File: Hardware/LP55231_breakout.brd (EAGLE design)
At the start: 22.9 x 30.5 mm, 29 parts, among them J1 To micro, J2 USER LED, J3 USER LED, J4 USER LED, U1 LP55231WQFN

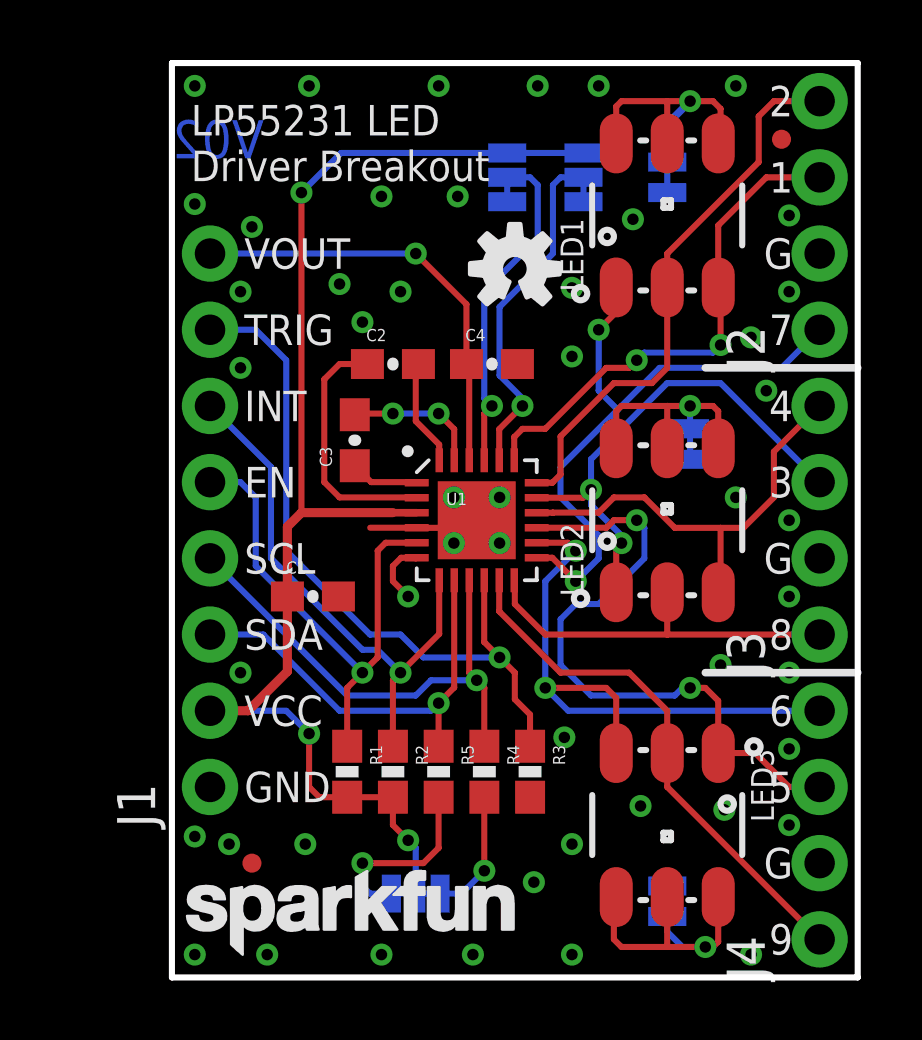
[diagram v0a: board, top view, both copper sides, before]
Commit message: Checklist updates for proto round 2.
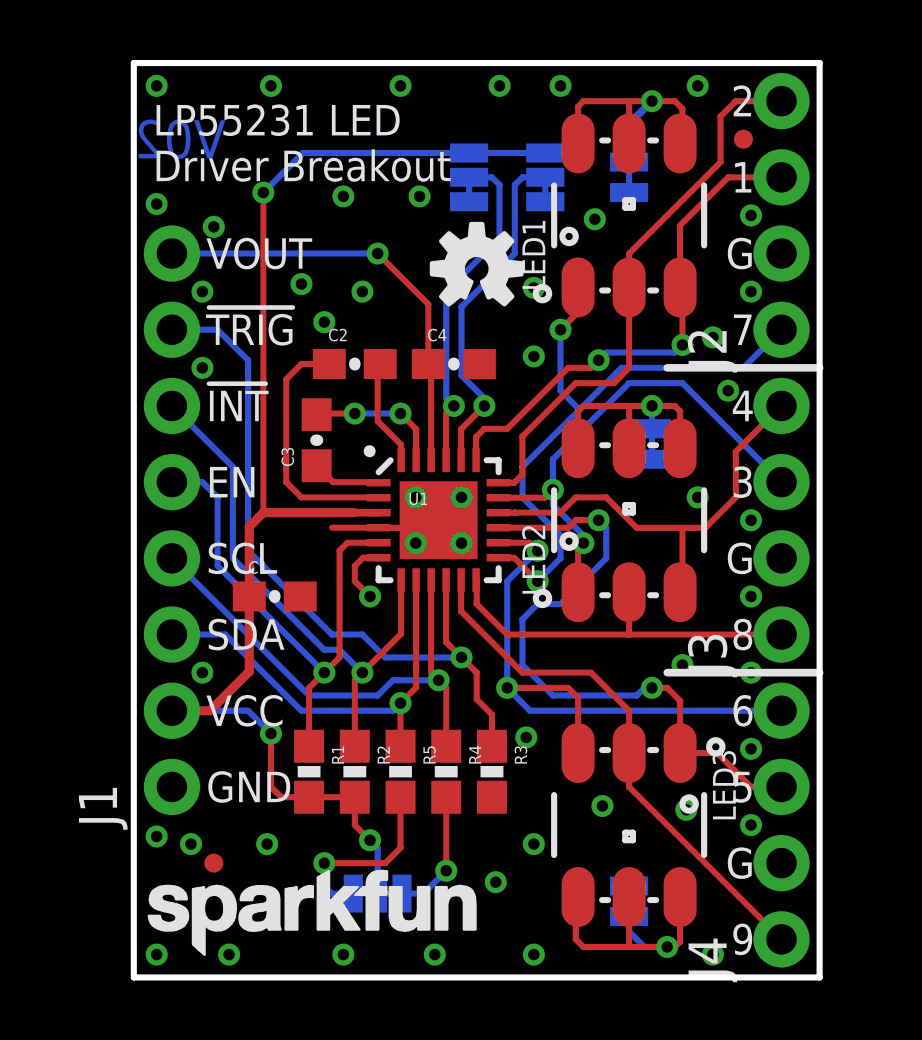
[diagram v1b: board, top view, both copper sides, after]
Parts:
- moved JP5 1.27 mm to (17.3, 17.8)
- moved C4 1.27 mm to (10.7, 20.4)
- moved JP3 1.27 mm to (13.7, 26.7)
- moved C1 1.27 mm to (4.70, 12.7)
- moved R1 1.27 mm to (5.84, 6.86)
- moved FD2 1.27 mm to (2.67, 3.81)
- moved J1 1.27 mm to (1.27, 6.35)
- moved LOGO1 1.27 mm to (3.43, 26.2)
- moved LOGO2 1.27 mm to (0.00, 0.25)
- moved C2 1.27 mm to (7.37, 20.4)
- moved C3 1.27 mm to (6.10, 17.9)
- moved FD1 1.27 mm to (20.3, 27.9)
- moved J2 1.27 mm to (21.6, 21.6)
- moved J3 1.27 mm to (21.6, 11.4)
- moved J4 1.27 mm to (21.6, 1.27)
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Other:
- board text added: "!INT"
- board text added: "!TRIG"
- board text removed: "INT"
- board text removed: "TRIG"

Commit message: Checklist review issues
Numbering of jumpers vs. comments got mismatched.
Now fixed.
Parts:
- JP2: value I2C-PULLUPS -> A0; device SparkFun-Passives:PAD-JUMPER-3-3OF3_NC_BY_TRACE_YES_SILK_FULL_BOX -> SparkFun-Passives:PAD-JUMPER-3-2OF3_NC_BY_TRACE_YES_SILK_FULL_BOX
- JP3: value A0 -> I2C-PULLUPS; device SparkFun-Passives:PAD-JUMPER-3-2OF3_NC_BY_TRACE_YES_SILK_FULL_BOX -> SparkFun-Passives:PAD-JUMPER-3-3OF3_NC_BY_TRACE_YES_SILK_FULL_BOX
- moved JP2 24.5 mm to (13.7, 26.7), turned to 270 degrees
- moved JP3 24.5 mm to (8.13, 2.79), turned to 180 degrees
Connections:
- net ADDR0: now also JP2.2; no longer JP3.2
- net GND: now also JP2.3; no longer JP3.3
- net N$21: now also JP3.1; no longer JP2.1
- net N$22: now also JP3.3; no longer JP2.3
- net VCC: now also JP2.1, JP3.2; no longer JP2.2, JP3.1
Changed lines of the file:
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@@
 <layer number="45" name="Holes" color="7" fill="1" visible="yes" active="yes"/>
 <layer number="46" name="Milling" color="3" fill="1" visible="no" active="yes"/>
-<layer number="47" name="Measures" color="7" fill="1" visible="yes" active="yes"/>
+<layer number="47" name="Measures" color="7" fill="1" visible="no" active="yes"/>
 <layer number="48" name="Document" color="7" fill="1" visible="no" active="yes"/>
 <layer number="49" name="Reference" color="7" fill="1" visible="no" active="yes"/>
@@
 <attribute name="SEE-ALSO" value="battery bayasitter" x="6.096" y="17.907" size="1.778" layer="27" rot="R90" display="off"/>
 </element>
-<element name="JP3" library="SparkFun-Passives" package="PAD-JUMPER-3-2OF3_NC_BY_TRACE_YES_SILK_FULL_BOX" value="A0" x="13.716" y="26.67" rot="MR270"/>
+<element name="JP2" library="SparkFun-Passives" package="PAD-JUMPER-3-2OF3_NC_BY_TRACE_YES_SILK_FULL_BOX" value="A0" x="13.716" y="26.67" rot="MR270"/>
 <element name="JP1" library="SparkFun-Passives" package="PAD-JUMPER-3-2OF3_NC_BY_TRACE_YES_SILK_FULL_BOX" value="A1" x="11.176" y="26.67" rot="MR270"/>
 <element name="LOGO3" library="SparkFun-Aesthetics" package="OSHW-LOGO-S" value="OSHW-LOGOS" x="11.43" y="23.622"/>
@@
 <attribute name="PROD_ID" value="CONN-09696" x="21.59" y="1.27" size="1.778" layer="27" font="vector" ratio="15" rot="R90" display="off"/>
 </element>
-<element name="JP2" library="SparkFun-Passives" package="PAD-JUMPER-3-3OF3_NC_BY_TRACE_YES_SILK_FULL_BOX" value="I2C-PULLUPS" x="8.128" y="2.794" rot="MR180"/>
+<element name="JP3" library="SparkFun-Passives" package="PAD-JUMPER-3-3OF3_NC_BY_TRACE_YES_SILK_FULL_BOX" value="I2C-PULLUPS" x="8.128" y="2.794" rot="MR180"/>
 <element name="R4" library="SparkFun-Resistors" package="0603-RES" value="4.7K" x="10.414" y="6.858" rot="R270">
 <attribute name="PROD_ID" value="RES-07857" x="10.414" y="6.858" size="1.778" layer="27" font="vector" ratio="15" rot="R270" display="off"/>
@@
 <contactref element="C1" pad="2"/>
 <contactref element="JP1" pad="3"/>
-<contactref element="JP3" pad="3"/>
+<contactref element="JP2" pad="3"/>
 <contactref element="J4" pad="2"/>
 <contactref element="J3" pad="2"/>
@@
 <contactref element="U1" pad="3"/>
 <contactref element="C1" pad="1"/>
-<contactref element="JP3" pad="1"/>
+<contactref element="JP2" pad="1"/>
 <contactref element="JP1" pad="1"/>
-<contactref element="JP2" pad="2"/>
+<contactref element="JP3" pad="2"/>
 <contactref element="J1" pad="2"/>
 <contactref element="R2" pad="2"/>
@@
 <signal name="ADDR0">
 <contactref element="U1" pad="20"/>
-<contactref element="JP3" pad="2"/>
+<contactref element="JP2" pad="2"/>
 <wire x1="10.922" y1="20.066" x2="10.922" y2="22.352" width="0.2032" layer="16"/>
 <wire x1="11.684" y1="19.304" x2="10.922" y2="20.066" width="0.2032" layer="16"/>
@@
 <signal name="N$21">
 <contactref element="R5" pad="2"/>
-<contactref element="JP2" pad="1"/>
+<contactref element="JP3" pad="1"/>
 <wire x1="8.89" y1="6.008" x2="8.89" y2="4.318" width="0.2032" layer="1"/>
 <wire x1="8.89" y1="4.318" x2="8.382" y2="3.81" width="0.2032" layer="1"/>
@@
 <signal name="N$22">
 <contactref element="R4" pad="2"/>
-<contactref element="JP2" pad="3"/>
+<contactref element="JP3" pad="3"/>
 <wire x1="10.414" y1="6.008" x2="10.414" y2="3.556" width="0.2032" layer="1"/>
 <via x="10.414" y="3.556" extent="1-16" drill="0.381"/>

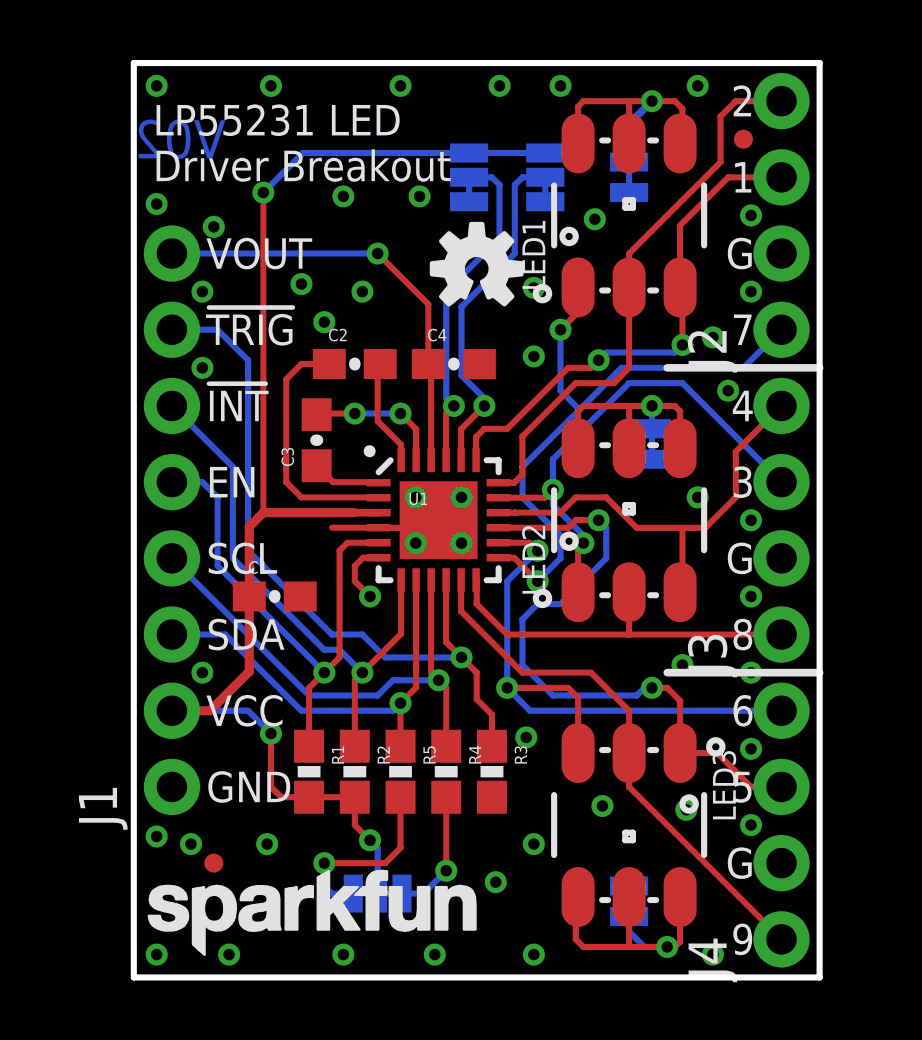
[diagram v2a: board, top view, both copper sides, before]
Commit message: Fixing RGB assignments of first LED.
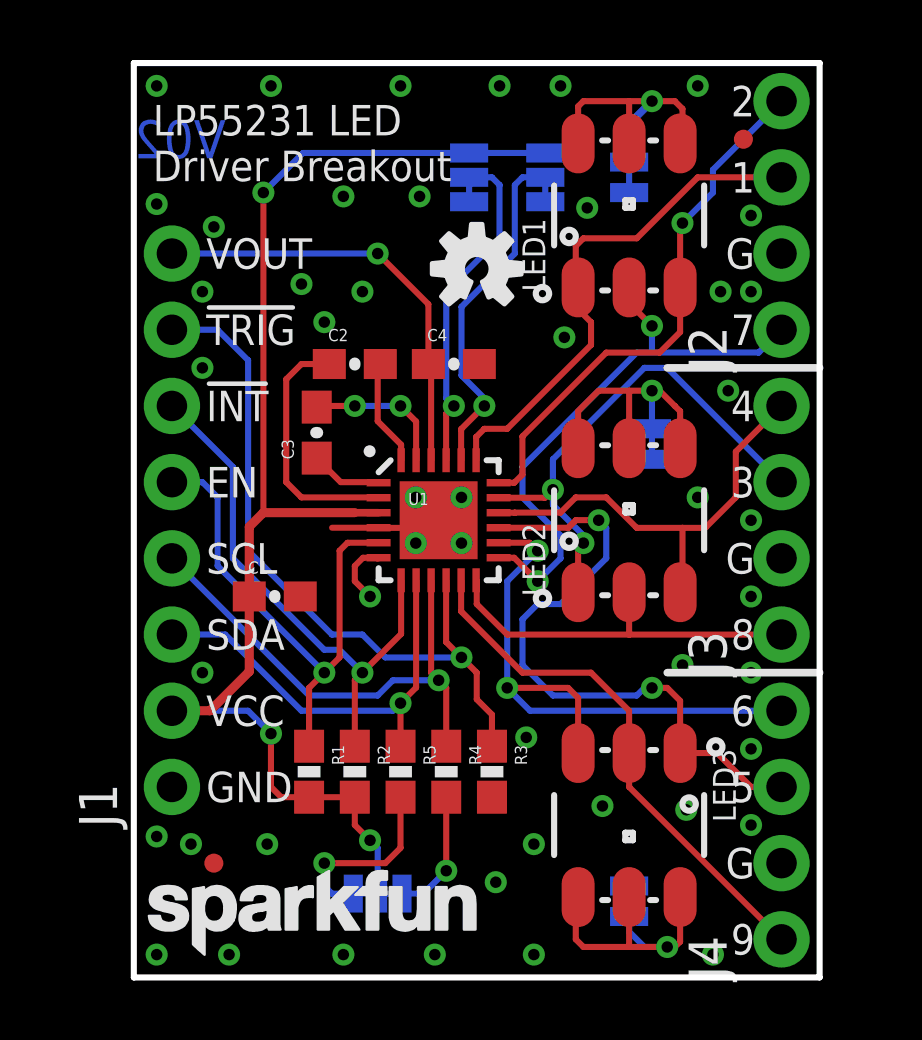
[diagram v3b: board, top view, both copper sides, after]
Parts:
- moved C3 0.25 mm to (6.10, 18.2)
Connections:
- net B1: now also LED1.3; no longer LED1.2
- net G1: now also LED1.1; no longer LED1.3
- net R1: now also LED1.2; no longer LED1.1
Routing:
- net R1: track 21.4 -> 19.3 mm
- net N$2: track 8.19 -> 9.62 mm
- net B1: track 18.6 -> 18.0 mm, vias 0 -> 1
- net G1: track 17.0 -> 17.2 mm, vias 2 -> 0
- net GND: vias 49 -> 48

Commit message: Rolling version number
From V02 to V03.
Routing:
- net GND: vias 48 -> 49
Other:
- board text added: "V03"
- board text removed: "V02"
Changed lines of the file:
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@@
 <setting verticaltext="up"/>
 </settings>
-<grid distance="0.01" unitdist="inch" unit="inch" style="lines" multiple="1" display="yes" altdistance="0.01" altunitdist="inch" altunit="inch"/>
+<grid distance="0.05" unitdist="inch" unit="inch" style="lines" multiple="1" display="yes" altdistance="0.005" altunitdist="inch" altunit="inch"/>
 <layers>
 <layer number="1" name="Top" color="4" fill="1" visible="yes" active="yes"/>
@@
 <layer number="19" name="Unrouted" color="6" fill="1" visible="yes" active="yes"/>
 <layer number="20" name="Dimension" color="15" fill="1" visible="yes" active="yes"/>
-<layer number="21" name="tPlace" color="16" fill="1" visible="yes" active="yes"/>
+<layer number="21" name="tPlace" color="16" fill="1" visible="no" active="yes"/>
 <layer number="22" name="bPlace" color="14" fill="1" visible="no" active="yes"/>
 <layer number="23" name="tOrigins" color="15" fill="1" visible="yes" active="yes"/>
@@
 <layer number="29" name="tStop" color="7" fill="3" visible="no" active="yes"/>
 <layer number="30" name="bStop" color="7" fill="6" visible="no" active="yes"/>
-<layer number="31" name="tCream" color="7" fill="4" visible="yes" active="yes"/>
+<layer number="31" name="tCream" color="7" fill="4" visible="no" active="yes"/>
 <layer number="32" name="bCream" color="7" fill="5" visible="no" active="yes"/>
 <layer number="33" name="tFinish" color="6" fill="3" visible="no" active="yes"/>
@@
 <layer number="49" name="Reference" color="7" fill="1" visible="no" active="yes"/>
 <layer number="50" name="dxf" color="7" fill="1" visible="no" active="no"/>
-<layer number="51" name="tDocu" color="6" fill="1" visible="no" active="yes"/>
+<layer number="51" name="tDocu" color="6" fill="1" visible="yes" active="yes"/>
 <layer number="52" name="bDocu" color="7" fill="1" visible="no" active="yes"/>
 <layer number="53" name="tGND_GNDA" color="7" fill="9" visible="no" active="no"/>
@@
 <text x="2.413" y="21.59" size="1.016" layer="21" font="vector" ratio="15" rot="R180" align="center-right">!TRIG</text>
 <text x="2.413" y="24.13" size="1.016" layer="21" font="vector" ratio="15" rot="R180" align="center-right">VOUT</text>
-<text x="0" y="27.94" size="1.27" layer="16" font="vector" ratio="15" rot="MR0" align="center-right">V02</text>
+<text x="0" y="27.94" size="1.27" layer="16" font="vector" ratio="15" rot="MR0" align="center-right">V03</text>
 <text x="2.413" y="8.89" size="1.016" layer="22" font="vector" ratio="15" rot="MR0" align="center-right">VCC</text>
 <text x="2.413" y="11.43" size="1.016" layer="22" font="vector" ratio="15" rot="MR0" align="center-right">SDA</text>
@@
 <via x="15.621" y="5.715" extent="1-16" drill="0.381"/>
 <via x="15.113" y="25.654" extent="1-16" drill="0.381"/>
+<via x="13.208" y="20.447" extent="1-16" drill="0.381"/>
 </signal>
 <signal name="VCC">
